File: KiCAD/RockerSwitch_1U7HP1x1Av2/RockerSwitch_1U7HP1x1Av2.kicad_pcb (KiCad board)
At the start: 2 copper layers, 35.2 x 39.7 mm, 7 parts, among them SW1 SW_SPDT_Rocker_Switch_Panel_M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

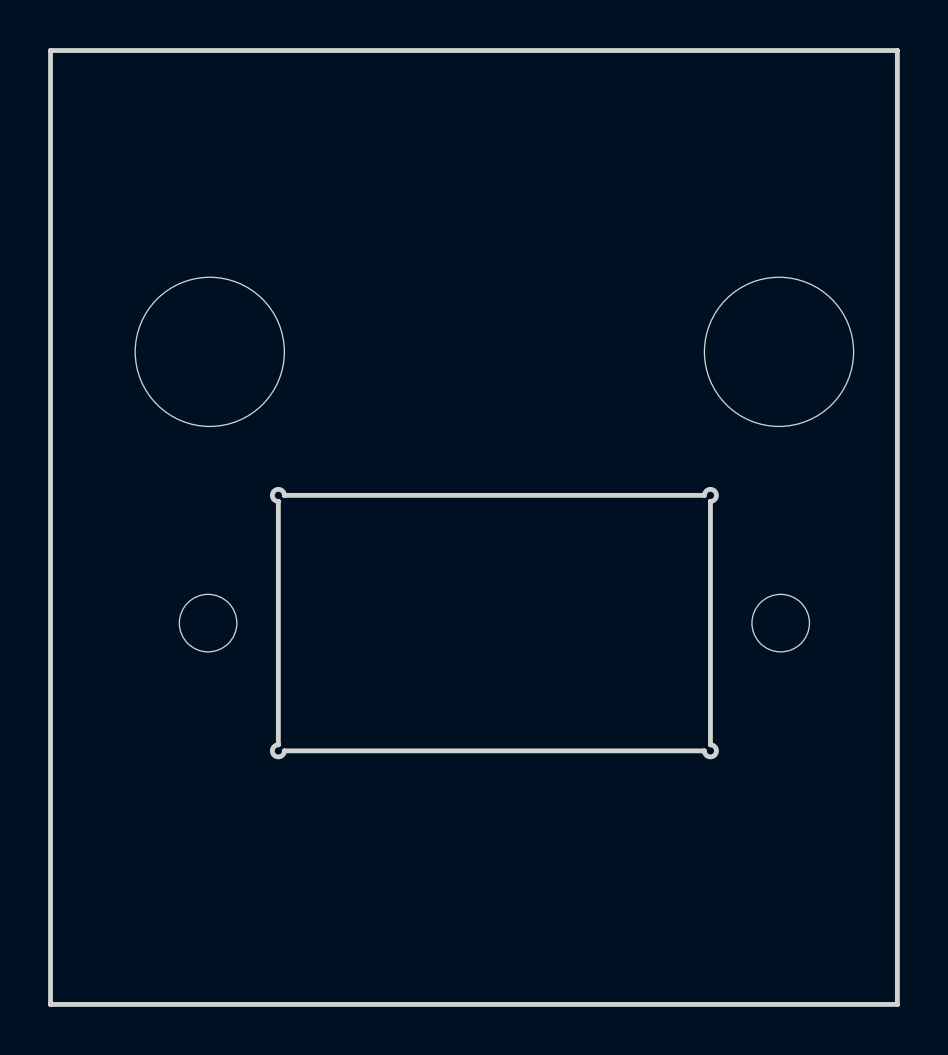
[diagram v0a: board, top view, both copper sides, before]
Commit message: updated all modules to use plated through-holes wherever possible
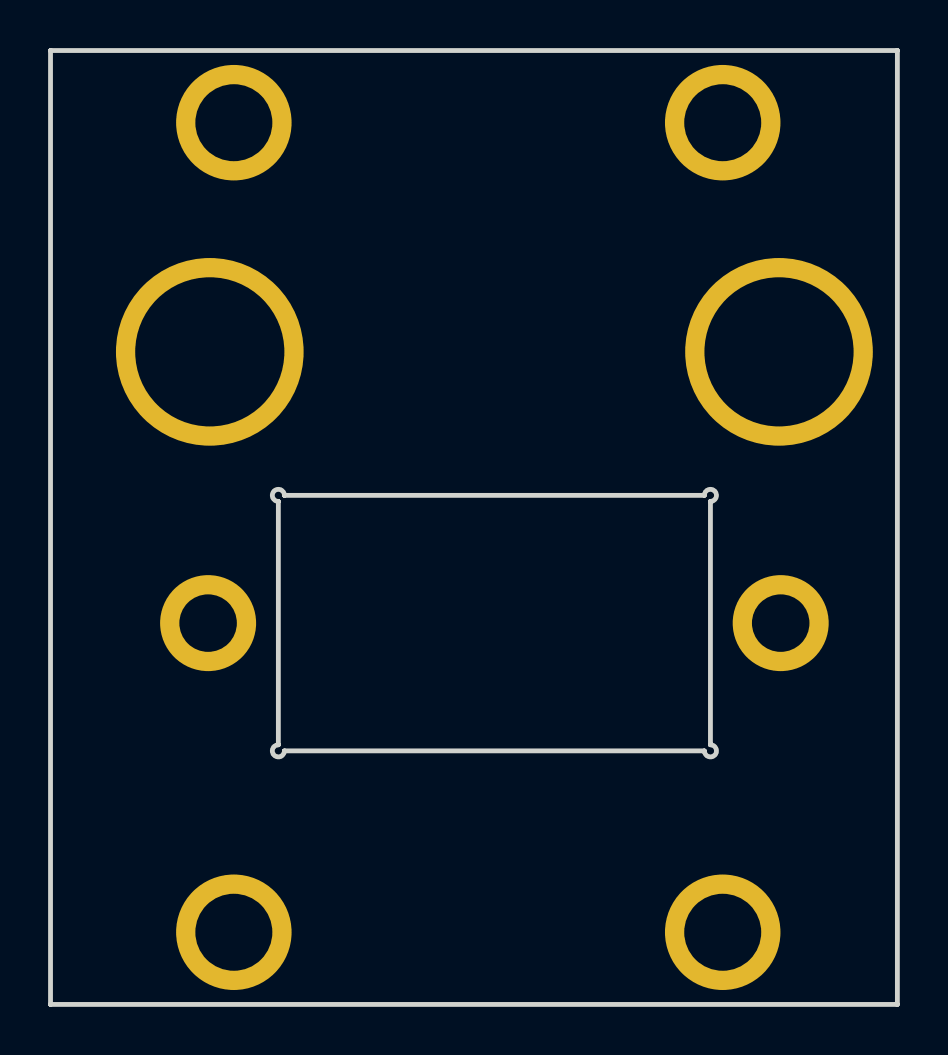
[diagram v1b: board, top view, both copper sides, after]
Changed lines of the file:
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@@
 			)
 		)
-		(pad "" np_thru_hole circle
+		(pad "" thru_hole circle
 			(at -11.9 0)
-			(size 2.39 2.39)
+			(size 3.99 3.99)
 			(drill 2.39)
 			(layers "*.Cu" "*.Mask")
-		)
-		(pad "" np_thru_hole circle
+			(remove_unused_layers no)
+		)
+		(pad "" thru_hole circle
 			(at 11.9 0)
-			(size 2.39 2.39)
+			(size 3.99 3.99)
 			(drill 2.39)
 			(layers "*.Cu" "*.Mask")
+			(remove_unused_layers no)
 		)
 		(embedded_fonts no)
@@
 			)
 		)
-		(pad "" np_thru_hole oval
+		(pad "" thru_hole circle
 			(at 0 0)
-			(size 4.34 3.2)
-			(drill oval 4.34 3.2)
-			(layers "*.Cu" "*.Mask")
+			(size 4.8 4.8)
+			(drill 3.2)
+			(layers "*.Cu" "*.Mask")
+			(remove_unused_layers no)
 		)
 		(embedded_fonts no)
@@
 			)
 		)
-		(pad "" np_thru_hole circle
+		(pad "" thru_hole circle
 			(at 0 0)
-			(size 6.2 6.2)
+			(size 7.8 7.8)
 			(drill 6.2)
 			(layers "*.Cu" "*.Mask")
+			(remove_unused_layers no)
 		)
 		(embedded_fonts no)
@@
 			)
 		)
-		(pad "" np_thru_hole oval
+		(pad "" thru_hole circle
 			(at 0 0)
-			(size 4.34 3.2)
-			(drill oval 4.34 3.2)
-			(layers "*.Cu" "*.Mask")
+			(size 4.8 4.8)
+			(drill 3.2)
+			(layers "*.Cu" "*.Mask")
+			(remove_unused_layers no)
 		)
 		(embedded_fonts no)
@@
 			)
 		)
-		(pad "" np_thru_hole circle
+		(pad "" thru_hole circle
 			(at 0 0)
-			(size 6.2 6.2)
+			(size 7.8 7.8)
 			(drill 6.2)
 			(layers "*.Cu" "*.Mask")
+			(remove_unused_layers no)
 		)
 		(embedded_fonts no)
@@
 			)
 		)
-		(pad "" np_thru_hole oval
+		(pad "" thru_hole circle
 			(at 0 0)
-			(size 4.34 3.2)
-			(drill oval 4.34 3.2)
-			(layers "*.Cu" "*.Mask")
+			(size 4.8 4.8)
+			(drill 3.2)
+			(layers "*.Cu" "*.Mask")
+			(remove_unused_layers no)
 		)
 		(embedded_fonts no)
@@
 			)
 		)
-		(pad "" np_thru_hole oval
+		(pad "" thru_hole circle
 			(at 0 0)
-			(size 4.34 3.2)
-			(drill oval 4.34 3.2)
-			(layers "*.Cu" "*.Mask")
+			(size 4.8 4.8)
+			(drill 3.2)
+			(layers "*.Cu" "*.Mask")
+			(remove_unused_layers no)
 		)
 		(embedded_fonts no)
